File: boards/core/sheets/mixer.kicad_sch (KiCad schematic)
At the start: 21 parts, among them U208 TL072

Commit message: Added schematics docs
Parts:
- renumbered TP206 to TP202
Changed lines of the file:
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@@
 		(on_board yes)
 		(dnp no)
-		(property "Reference" "TP206"
+		(property "Reference" "TP202"
 			(at 200.66 85.725 0)
 			(effects

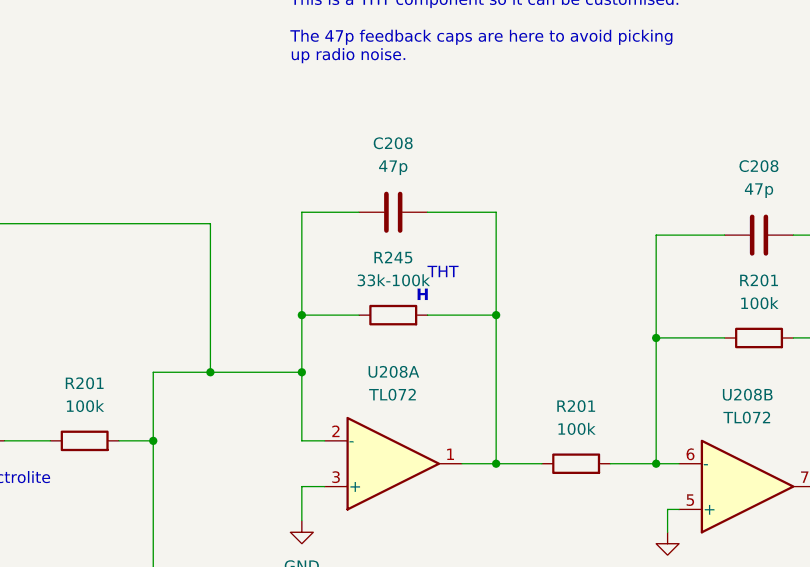
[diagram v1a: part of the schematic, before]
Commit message: Replaced mixer feedback resistor to SMD
https://github.com/shmoergh/hog/issues/9
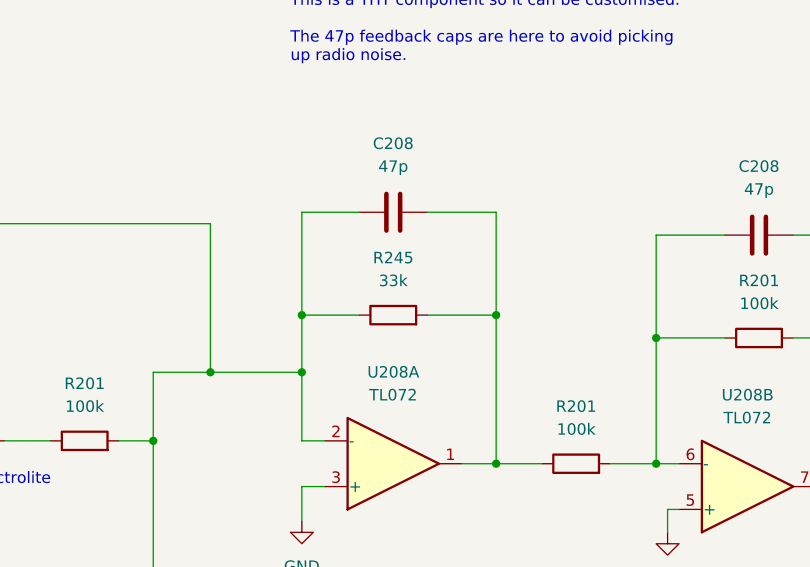
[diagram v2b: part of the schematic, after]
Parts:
- R245: value 33k-100k -> 33k; footprint Shmoergh_Custom_Footprints:R_Axial_DIN0207_L6.3mm_D2.5mm_P7.62mm_Horizontal -> Resistor_SMD:R_0603_1608Metric; LCSC (none) -> C4216; now in the parts list
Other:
- note removed: "THT"
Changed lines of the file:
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@@
-	(text "H"
-		(exclude_from_sim no)
-		(at 152.4 57.15 0)
-		(effects
-			(font
-				(size 1.27 1.27)
-				(thickness 0.254)
-				(bold yes)
-				(color 255 0 221 1)
-			)
-			(justify left bottom)
-		)
-	)
-	(text "THT"
-		(exclude_from_sim no)
-		(at 153.67 54.61 0)
-		(effects
-			(font
-				(size 1.27 1.27)
-			)
-			(justify left bottom)
-		)
-	)
 	(text "H"
 		(exclude_from_sim no)
@@
 	(symbol
 		(lib_id "Device:R")
+		(at 149.86 58.42 90)
+		(unit 1)
+		(exclude_from_sim no)
+		(in_bom yes)
+		(on_board yes)
+		(dnp no)
+		(property "Reference" "R245"
+			(at 149.86 52.07 90)
+			(effects
+				(font
+					(size 1.27 1.27)
+				)
+			)
+		)
+		(property "Value" "33k"
+			(at 149.86 54.61 90)
+			(effects
+				(font
+					(size 1.27 1.27)
+				)
+			)
+		)
+		(property "Footprint" "Resistor_SMD:R_0603_1608Metric"
+			(at 149.86 60.198 90)
+			(effects
+				(font
+					(size 1.27 1.27)
+				)
+				(hide yes)
+			)
+		)
+		(property "Datasheet" "~"
+			(at 149.86 58.42 0)
+			(effects
+				(font
+					(size 1.27 1.27)
+				)
+				(hide yes)
+			)
+		)
+		(property "Description" ""
+			(at 149.86 58.42 0)
+			(effects
+				(font
+					(size 1.27 1.27)
+				)
+				(hide yes)
+			)
+		)
+		(property "LCSC" "C4216"
+			(at 149.86 58.42 90)
+			(effects
+				(font
+					(size 1.27 1.27)
+				)
+				(hide yes)
+			)
+		)
+		(pin "1"
+		)
+		(pin "2"
+		)
+		(instances
+			(project "core"
+				(path "/91ae1fff-f2ac-4868-8c3f-8c5c03d8b2f6/865c0c7b-5b14-44d4-94d3-6e86ffb26d5b"
+					(reference "R245")
+					(unit 1)
+				)
+			)
+		)
+	)
+	(symbol
+		(lib_id "Device:R")
 		(at 190.5 60.96 90)
 		(unit 1)
@@
 					(unit 1)
 				)
-			)
-		)
-	)
-	(symbol
-		(lib_id "Device:R")
-		(at 149.86 58.42 90)
-		(unit 1)
-		(exclude_from_sim no)
-		(in_bom no)
-		(on_board yes)
-		(dnp no)
-		(fields_autoplaced yes)
-		(property "Reference" "R245"
-			(at 149.86 52.07 90)
-			(effects
-				(font
-					(size 1.27 1.27)
-				)
-			)
-		)
-		(property "Value" "33k-100k"
-			(at 149.86 54.61 90)
-			(effects
-				(font
-					(size 1.27 1.27)
-				)
-			)
-		)
-		(property "Footprint" "Shmoergh_Custom_Footprints:R_Axial_DIN0207_L6.3mm_D2.5mm_P7.62mm_Horizontal"
-			(at 149.86 60.198 90)
-			(effects
-				(font
-					(size 1.27 1.27)
-				)
-				(hide yes)
-			)
-		)
-		(property "Datasheet" "~"
-			(at 149.86 58.42 0)
-			(effects
-				(font
-					(size 1.27 1.27)
-				)
-				(hide yes)
-			)
-		)
-		(property "Description" ""
-			(at 149.86 58.42 0)
-			(effects
-				(font
-					(size 1.27 1.27)
-				)
-				(hide yes)
-			)
-		)
-		(pin "1"
-		)
-		(pin "2"
-		)
-		(instances
-			(project "core-rev-3"
-				(path "/91ae1fff-f2ac-4868-8c3f-8c5c03d8b2f6/865c0c7b-5b14-44d4-94d3-6e86ffb26d5b"
-					(reference "R245")
-					(unit 1)
-				)

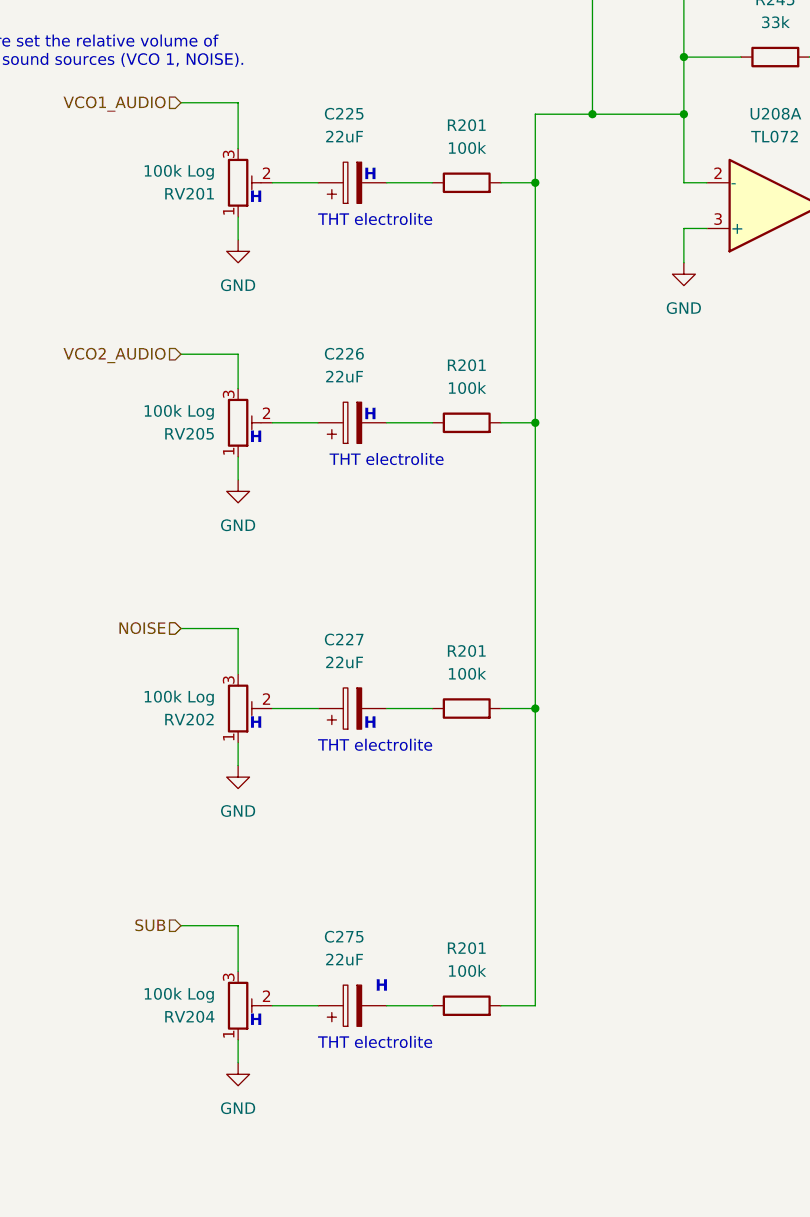
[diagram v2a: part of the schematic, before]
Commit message: Replaced mixer input caps to SMD
https://github.com/shmoergh/hog/issues/26
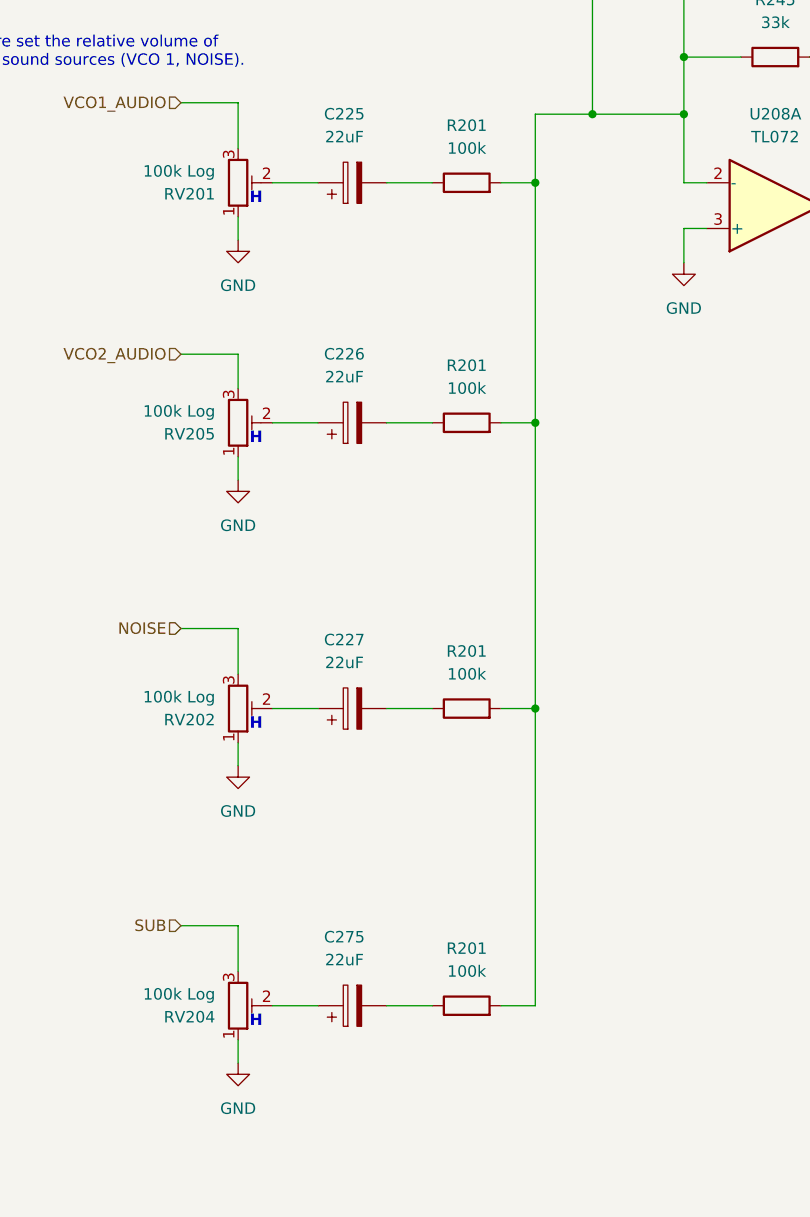
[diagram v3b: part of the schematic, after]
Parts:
- C225, C226, C227, C275: footprint Capacitor_THT:CP_Radial_D6.3mm_P2.50mm -> Capacitor_SMD:CP_Elec_6.3x5.4; LCSC (none) -> C3001241
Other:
- note removed: "THT electrolite"
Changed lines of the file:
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@@
-		)
-	)
-	(text "THT electrolite"
-		(exclude_from_sim no)
-		(at 99.06 168.91 0)
-		(effects
-			(font
-				(size 1.27 1.27)
-			)
-			(justify left bottom)
-		)
-	)
-	(text "THT electrolite"
-		(exclude_from_sim no)
-		(at 99.06 135.89 0)
-		(effects
-			(font
-				(size 1.27 1.27)
-			)
-			(justify left bottom)
-		)
-	)
-	(text "H"
-		(exclude_from_sim no)
-		(at 104.14 99.06 0)
-		(effects
-			(font
-				(size 1.27 1.27)
-				(thickness 0.254)
-				(bold yes)
-				(color 255 0 221 1)
-			)
-			(justify left bottom)
-		)
-	)
-	(text "THT electrolite"
-		(exclude_from_sim no)
-		(at 100.33 104.14 0)
-		(effects
-			(font
-				(size 1.27 1.27)
-			)
-			(justify left bottom)
 		)
 	)
@@
 	(text "H"
 		(exclude_from_sim no)
-		(at 104.14 133.35 0)
-		(effects
-			(font
-				(size 1.27 1.27)
-				(thickness 0.254)
-				(bold yes)
-				(color 255 0 221 1)
-			)
-			(justify left bottom)
-		)
-	)
-	(text "H"
-		(exclude_from_sim no)
-		(at 105.41 162.56 0)
-		(effects
-			(font
-				(size 1.27 1.27)
-				(thickness 0.254)
-				(bold yes)
-				(color 255 0 221 1)
-			)
-			(justify left bottom)
-		)
-	)
-	(text "H"
-		(exclude_from_sim no)
 		(at 91.44 74.93 0)
 		(effects
@@
 		)
 	)
-	(text "THT electrolite"
-		(exclude_from_sim no)
-		(at 99.06 77.47 0)
-		(effects
-			(font
-				(size 1.27 1.27)
-			)
-			(justify left bottom)
-		)
-	)
-	(text "H"
-		(exclude_from_sim no)
-		(at 104.14 72.39 0)
-		(effects
-			(font
-				(size 1.27 1.27)
-				(thickness 0.254)
-				(bold yes)
-				(color 255 0 221 1)
-			)
-			(justify left bottom)
-		)
-	)
 	(text "H"
 		(exclude_from_sim no)
@@
 			)
 		)
-		(property "Footprint" "Capacitor_THT:CP_Radial_D6.3mm_P2.50mm"
+		(property "Footprint" "Capacitor_SMD:CP_Elec_6.3x5.4"
 			(at 106.68 162.8648 0)
 			(effects
@@
 		(property "Description" ""
 			(at 102.87 163.83 0)
+			(effects
+				(font
+					(size 1.27 1.27)
+				)
+				(hide yes)
+			)
+		)
+		(property "LCSC" "C3001241"
+			(at 102.87 163.83 90)
 			(effects
 				(font
@@
 			)
 		)
-		(property "Footprint" "Capacitor_THT:CP_Radial_D6.3mm_P2.50mm"
+		(property "Footprint" "Capacitor_SMD:CP_Elec_6.3x5.4"
 			(at 106.68 98.0948 0)
 			(effects
@@
 		(property "Description" ""
 			(at 102.87 99.06 0)
+			(effects
+				(font
+					(size 1.27 1.27)
+				)
+				(hide yes)
+			)
+		)
+		(property "LCSC" "C3001241"
+			(at 102.87 99.06 90)
 			(effects
 				(font
@@
 			)
 		)
-		(property "Footprint" "Capacitor_THT:CP_Radial_D6.3mm_P2.50mm"
+		(property "Footprint" "Capacitor_SMD:CP_Elec_6.3x5.4"
 			(at 106.68 71.4248 0)
 			(effects
@@
 		(property "Description" ""
 			(at 102.87 72.39 0)
+			(effects
+				(font
+					(size 1.27 1.27)
+				)
+				(hide yes)
+			)
+		)
+		(property "LCSC" "C3001241"
+			(at 102.87 72.39 90)
 			(effects
 				(font
@@
 			)
 		)
-		(property "Footprint" "Capacitor_THT:CP_Radial_D6.3mm_P2.50mm"
+		(property "Footprint" "Capacitor_SMD:CP_Elec_6.3x5.4"
 			(at 106.68 129.8448 0)
 			(effects
@@
 			(effects
 				(font
+					(size 1.27 1.27)
+				)
+				(hide yes)
+			)
+		)
+		(property "LCSC" "C3001241"
+			(at 102.87 130.81 90)
+			(effects
+				(font
